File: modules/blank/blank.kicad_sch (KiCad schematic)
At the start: 2 parts

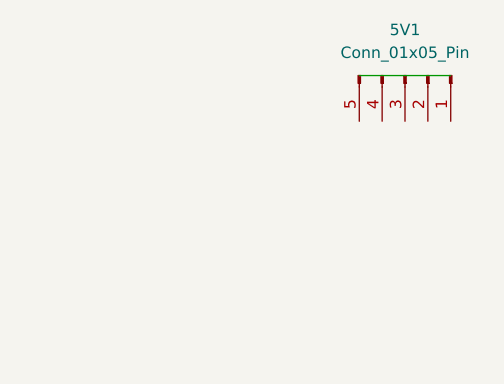
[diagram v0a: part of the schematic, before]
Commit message: Fixed some pcb layout issues.
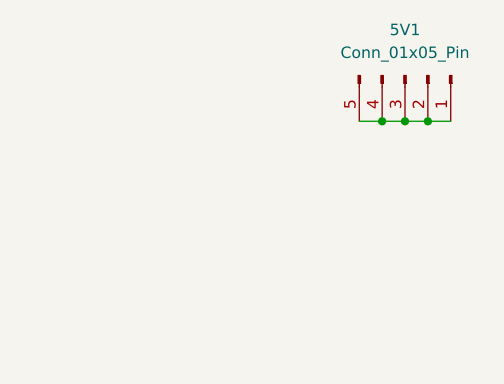
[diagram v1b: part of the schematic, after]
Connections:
- net at 5V1.1 (Pin_1): now also 5V1.2 (Pin_2), 5V1.3 (Pin_3), 5V1.4 (Pin_4), 5V1.5 (Pin_5)
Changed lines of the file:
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@@
+	)
+	(junction
+		(at 139.7 40.64)
+		(diameter 0)
+		(color 0 0 0 0)
 	)
 	(junction
 		(at 38.1 125.73)
+		(diameter 0)
+		(color 0 0 0 0)
+	)
+	(junction
+		(at 144.78 40.64)
+		(diameter 0)
+		(color 0 0 0 0)
+	)
+	(junction
+		(at 142.24 40.64)
 		(diameter 0)
 		(color 0 0 0 0)
@@
 	(wire
 		(pts
-			(xy 137.16 35.56) (xy 147.32 35.56)
+			(xy 137.16 40.64) (xy 139.7 40.64)
 		)
 		(stroke
@@
 	(wire
 		(pts
+			(xy 139.7 40.64) (xy 142.24 40.64)
+		)
+		(stroke
+			(width 0)
+			(type default)
+		)
+	)
+	(wire
+		(pts
 			(xy 38.1 125.73) (xy 40.64 125.73)
 		)
 		(stroke
+			(width 0)
+			(type default)
+		)
+	)
+	(wire
+		(pts
+			(xy 144.78 40.64) (xy 147.32 40.64)
+		)
+		(stroke
+			(width 0)
+			(type default)
+		)
+	)
+	(wire
+		(pts
+			(xy 142.24 40.64) (xy 144.78 40.64)
+		)
+		(stroke

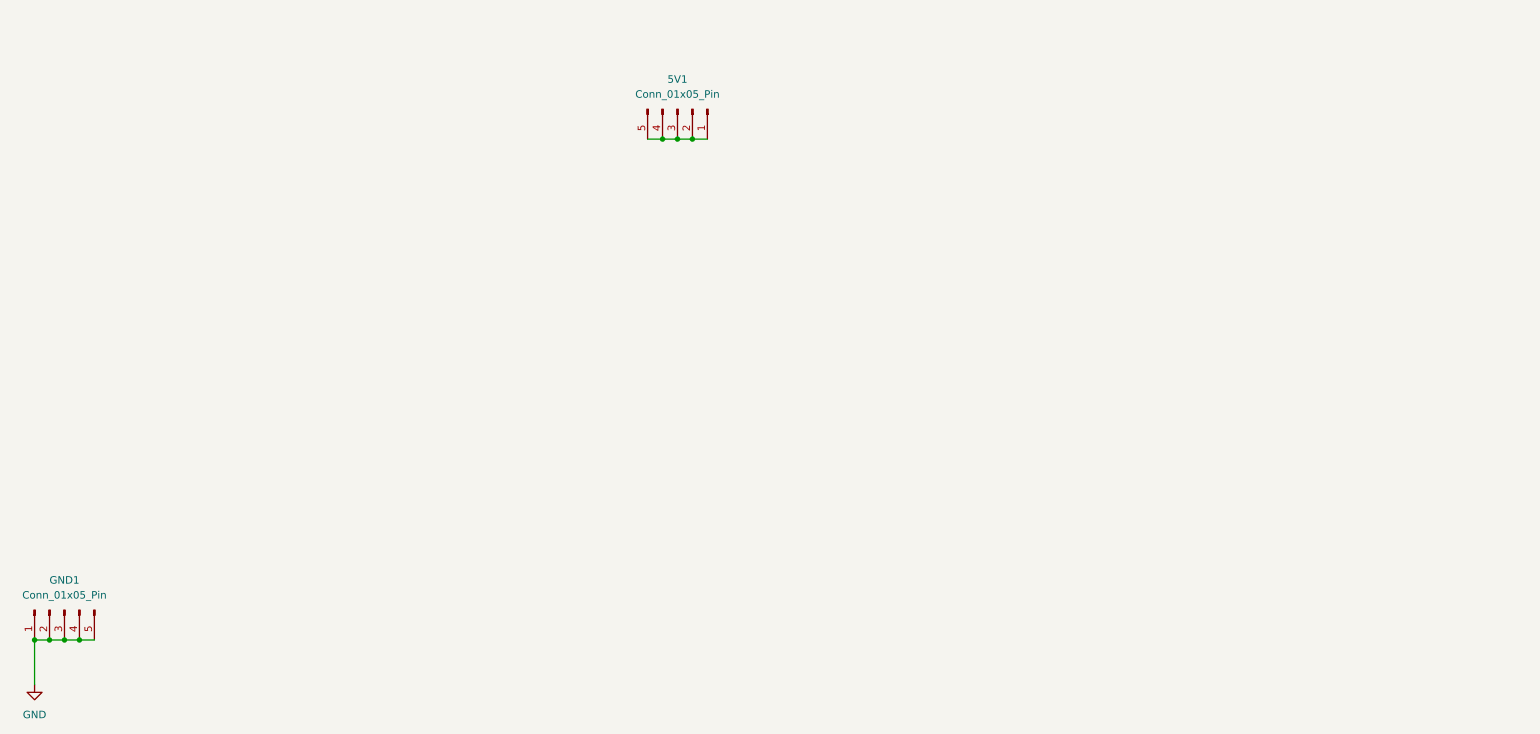
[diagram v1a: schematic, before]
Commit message: Add sockets for the blank project.
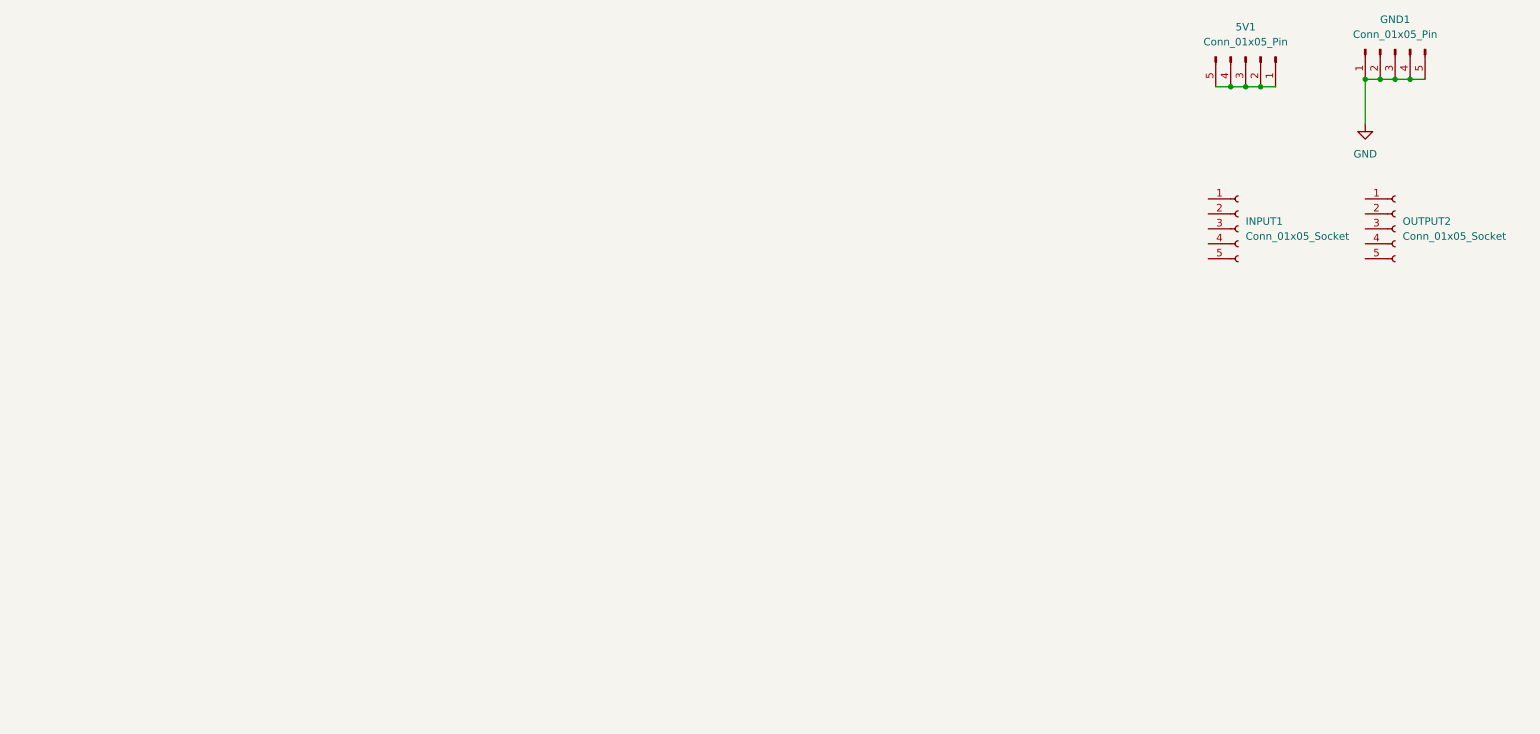
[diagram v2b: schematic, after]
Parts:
- added INPUT1, OUTPUT2: Conn_01x05_Socket, Connector_PinSocket_2.54mm:PinSocket_1x05_P2.54mm_Vertical, symbol Connector:Conn_01x05_Socket
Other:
- moved on the sheet: 5V1, GND1

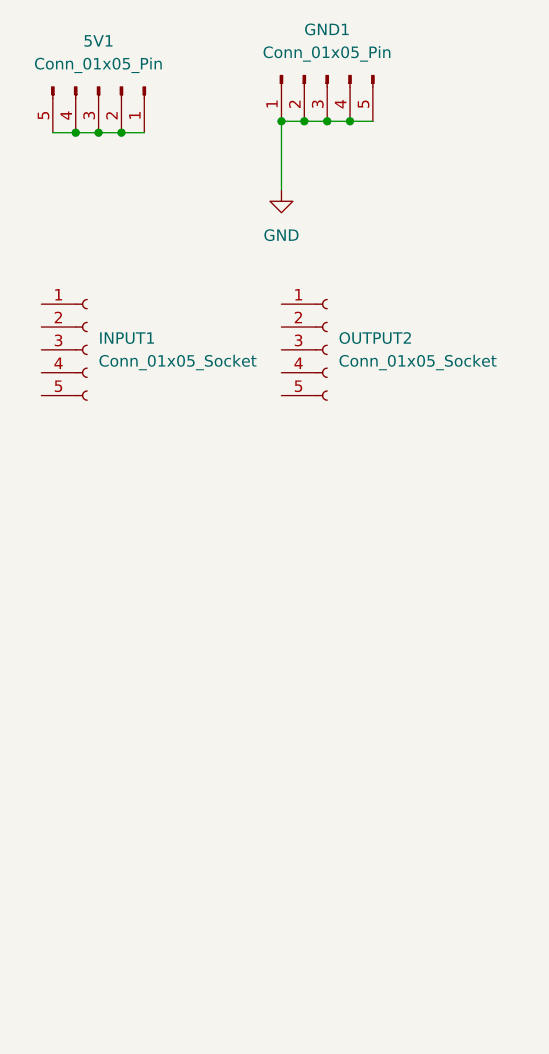
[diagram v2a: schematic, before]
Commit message: Update the basic kidcad app Add simulation support Introduce the version number silkscreen
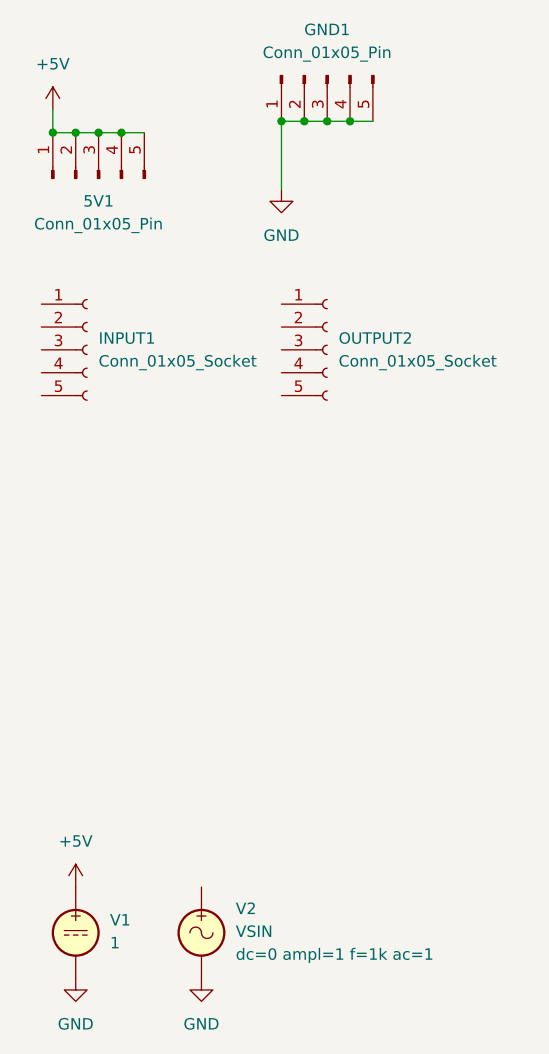
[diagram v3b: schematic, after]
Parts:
- added V1: 1, symbol Simulation_SPICE:VDC
- added V2: VSIN, symbol Simulation_SPICE:VSIN
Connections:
- net GND: now also V1.2, V2.2
- net +5V: now reaches 5V1.1 (Pin_1), 5V1.2 (Pin_2), 5V1.3 (Pin_3), 5V1.4 (Pin_4), 5V1.5 (Pin_5)
- net +5V: now also V1.1
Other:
- moved on the sheet: 5V1

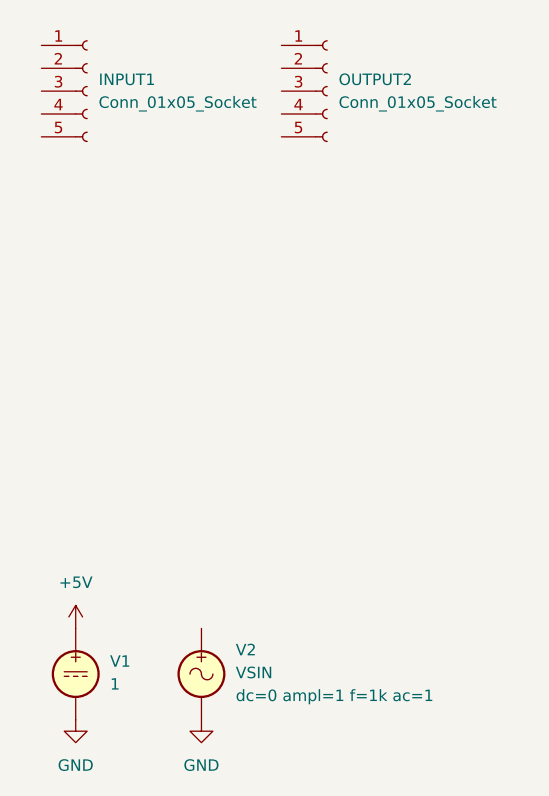
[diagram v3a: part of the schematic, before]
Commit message: Update the blank module with more details.
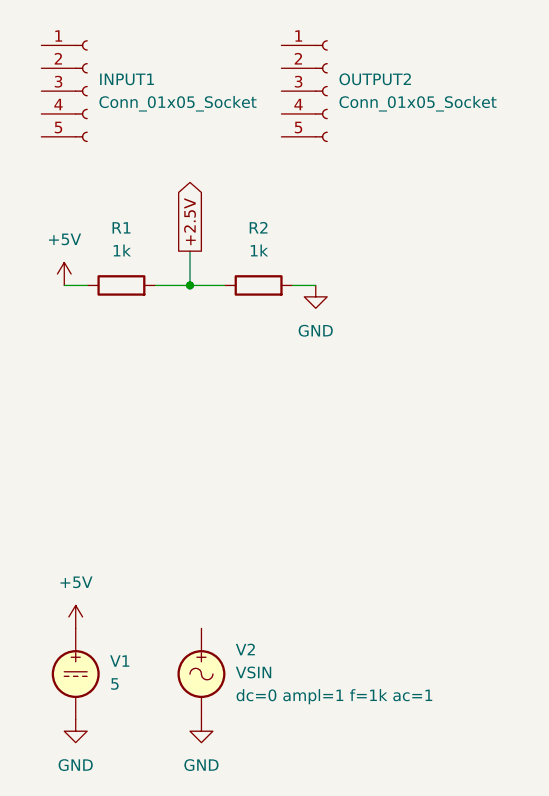
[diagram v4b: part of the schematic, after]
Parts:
- added R1, R2: 1k, symbol Device:R
- V1: value 1 -> 5
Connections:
- net +5V: now also R1.1
- net GND: now also R2.2
- new net +2.5V: R1.2, R2.1

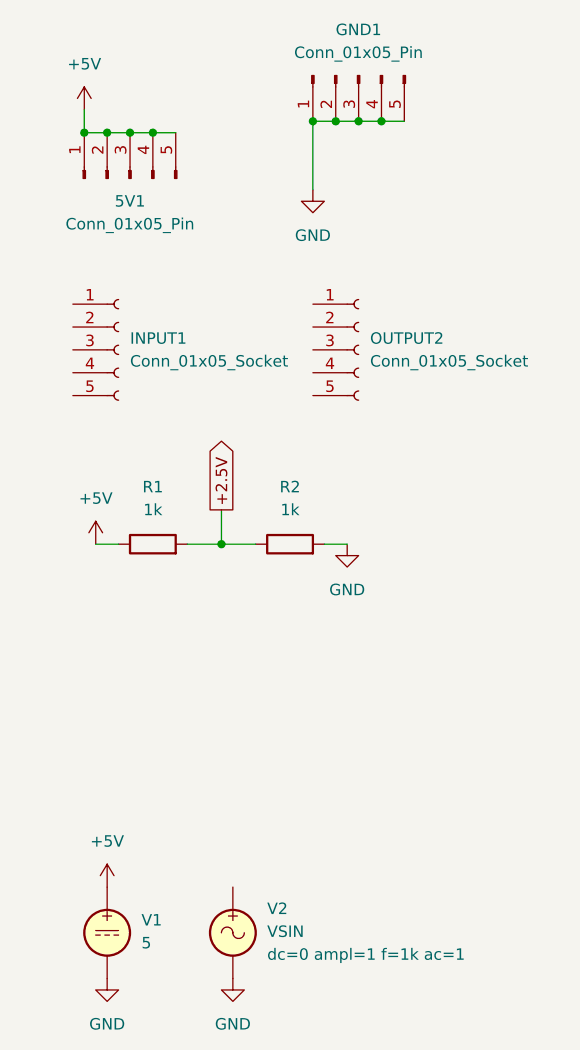
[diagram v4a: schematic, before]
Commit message: Update the blank module.
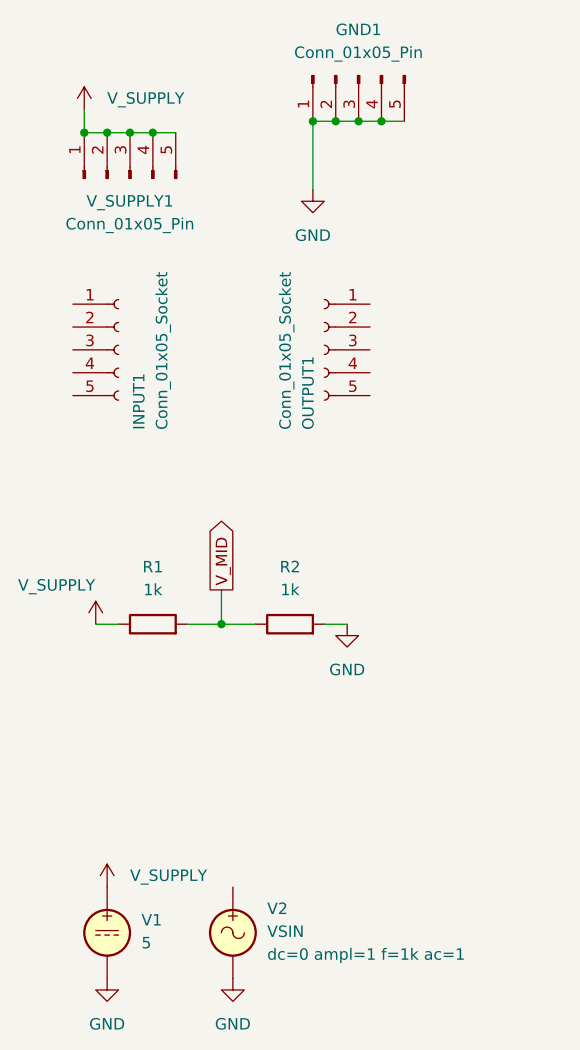
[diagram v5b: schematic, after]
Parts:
- GND1: footprint Connector_PinHeader_2.54mm:PinHeader_1x05_P2.54mm_Vertical -> BreadModular_MISC:Power_Connector
- V_SUPPLY1: renamed from 5V1; footprint Connector_PinHeader_2.54mm:PinHeader_1x05_P2.54mm_Vertical -> BreadModular_MISC:Power_Connector
- renumbered OUTPUT2 to OUTPUT1
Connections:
- net +2.5V renamed V_MID
- net +5V renamed V_SUPPLY
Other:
- moved on the sheet: OUTPUT1, R1, R2
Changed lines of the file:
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@@
 	)
 	(junction
-		(at 248.92 77.47)
+		(at 248.92 86.36)
 		(diameter 0)
 		(color 0 0 0 0)
@@
 	(wire
 		(pts
-			(xy 248.92 73.66) (xy 248.92 77.47)
-		)
-		(stroke
-			(width 0)
-			(type default)
-		)
-	)
-	(wire
-		(pts
-			(xy 248.92 77.47) (xy 252.73 77.47)
+			(xy 248.92 82.55) (xy 248.92 86.36)
+		)
+		(stroke
+			(width 0)
+			(type default)
+		)
+	)
+	(wire
+		(pts
+			(xy 248.92 86.36) (xy 252.73 86.36)
 		)
 		(stroke
@@
 	(wire
 		(pts
-			(xy 262.89 77.47) (xy 260.35 77.47)
+			(xy 262.89 86.36) (xy 260.35 86.36)
 		)
 		(stroke
@@
 	(wire
 		(pts
-			(xy 234.95 77.47) (xy 237.49 77.47)
+			(xy 234.95 86.36) (xy 237.49 86.36)
 		)
 		(stroke
@@
 	(wire
 		(pts
-			(xy 245.11 77.47) (xy 248.92 77.47)
+			(xy 245.11 86.36) (xy 248.92 86.36)
 		)
 		(stroke
@@
 		)
 	)
-	(global_label "+2.5V"
+	(global_label "V_MID"
 		(shape output)
-		(at 248.92 73.66 90)
+		(at 248.92 82.55 90)
 		(fields_autoplaced yes)
 		(effects
@@
 		)
 		(property "Intersheetrefs" "${INTERSHEET_REFS}"
-			(at 248.92 64.99 90)
+			(at 248.92 74.1824 90)
 			(effects
 				(font
@@
 	(symbol
 		(lib_id "Device:R")
-		(at 241.3 77.47 90)
+		(at 241.3 86.36 90)
 		(unit 1)
 		(exclude_from_sim no)
@@
 		(fields_autoplaced yes)
 		(property "Reference" "R1"
-			(at 241.3 71.12 90)
+			(at 241.3 80.01 90)
 			(effects
 				(font
@@
 		)
 		(property "Value" "1k"
-			(at 241.3 73.66 90)
+			(at 241.3 82.55 90)
 			(effects
 				(font
@@
 		)
 		(property "Footprint" ""
-			(at 241.3 79.248 90)
+			(at 241.3 88.138 90)
 			(effects
 				(font
@@
 		)
 		(property "Datasheet" "~"
-			(at 241.3 77.47 0)
+			(at 241.3 86.36 0)
 			(effects
 				(font
@@
 		)
 		(property "Description" "Resistor"
-			(at 241.3 77.47 0)
+			(at 241.3 86.36 0)
 			(effects
 				(font
@@
 		(dnp no)
 		(fields_autoplaced yes)
-		(property "Reference" "5V1"
+		(property "Reference" "V_SUPPLY1"
 			(at 238.76 39.37 90)
 			(effects
@@
 			)
 		)
-		(property "Footprint" "Connector_PinHeader_2.54mm:PinHeader_1x05_P2.54mm_Vertical"
+		(property "Footprint" "BreadModular_MISC:Power_Connector"
 			(at 238.76 36.83 0)
 			(effects
@@
 			(project ""
 				(path "/b63493d3-5f6d-47e3-845b-87e7090fc1ab"
-					(reference "5V1")
+					(reference "V_SUPPLY1")
 					(unit 1)
 				)
@@
 			)
 		)
-		(property "Value" "+5V"
-			(at 236.22 110.49 0)
-			(effects
-				(font
-					(size 1.27 1.27)
-				)
+		(property "Value" "V_SUPPLY"
+			(at 238.76 114.2999 0)
+			(effects
+				(font
+					(size 1.27 1.27)
+				)
+				(justify left)
 			)
 		)
@@
 			)
 		)
-		(property "Value" "+5V"
-			(at 233.68 24.13 0)
-			(effects
-				(font
-					(size 1.27 1.27)
-				)
+		(property "Value" "V_SUPPLY"
+			(at 236.22 27.9399 0)
+			(effects
+				(font
+					(size 1.27 1.27)
+				)
+				(justify left)
 			)
 		)
@@
 	(symbol
 		(lib_id "Connector:Conn_01x05_Socket")
-		(at 264.16 55.88 0)
+		(at 260.35 55.88 0)
+		(mirror y)
 		(unit 1)
 		(exclude_from_sim yes)
@@
 		(on_board yes)
 		(dnp no)
-		(fields_autoplaced yes)
-		(property "Reference" "OUTPUT2"
-			(at 265.43 54.6099 0)
+		(property "Reference" "OUTPUT1"
+			(at 258.572 64.77 90)
 			(effects
 				(font
@@
 		)
 		(property "Value" "Conn_01x05_Socket"
-			(at 265.43 57.1499 0)
+			(at 256.032 64.77 90)
 			(effects
 				(font
@@
 		)
 		(property "Footprint" "Connector_PinSocket_2.54mm:PinSocket_1x05_P2.54mm_Vertical"
-			(at 264.16 55.88 0)
+			(at 260.35 55.88 0)
 			(effects
 				(font
@@
 		)
 		(property "Datasheet" "~"
-			(at 264.16 55.88 0)
+			(at 260.35 55.88 0)
 			(effects
 				(font
@@
 		)
 		(property "Description" "Generic connector, single row, 01x05, script generated"
-			(at 264.16 55.88 0)
+			(at 260.35 55.88 0)
 			(effects
 				(font
@@
 			(project "blank"
 				(path "/b63493d3-5f6d-47e3-845b-87e7090fc1ab"
-					(reference "OUTPUT2")
+					(reference "OUTPUT1")
 					(unit 1)
 				)
@@
 	(symbol
 		(lib_id "power:GND")
-		(at 262.89 77.47 0)
+		(at 262.89 86.36 0)
 		(unit 1)
 		(exclude_from_sim no)
@@
 		(dnp no)
 		(property "Reference" "#PWR07"
-			(at 262.89 83.82 0)
+			(at 262.89 92.71 0)
 			(effects
 				(font
@@
 		)
 		(property "Value" "GND"
-			(at 262.89 82.55 0)
+			(at 262.89 91.44 0)
 			(effects
 				(font
@@
 		)
 		(property "Footprint" ""
-			(at 262.89 77.47 0)
+			(at 262.89 86.36 0)
 			(effects
 				(font
@@
 		)
 		(property "Datasheet" ""
-			(at 262.89 77.47 0)
+			(at 262.89 86.36 0)
 			(effects
 				(font
@@
 		)
 		(property "Description" "Power symbol creates a global label with name \"GND\" , ground"
-			(at 262.89 77.47 0)
+			(at 262.89 86.36 0)
 			(effects
 				(font
@@
 	(symbol
 		(lib_id "Device:R")
-		(at 256.54 77.47 90)
+		(at 256.54 86.36 90)
 		(unit 1)
 		(exclude_from_sim no)
@@
 		(fields_autoplaced yes)
 		(property "Reference" "R2"
-			(at 256.54 71.12 90)
+			(at 256.54 80.01 90)
 			(effects
 				(font
@@
 		)
 		(property "Value" "1k"
-			(at 256.54 73.66 90)
+			(at 256.54 82.55 90)
 			(effects
 				(font
@@
 		)
 		(property "Footprint" ""
-			(at 256.54 79.248 90)
+			(at 256.54 88.138 90)
 			(effects
 				(font
@@
 		)
 		(property "Datasheet" "~"
-			(at 256.54 77.47 0)
+			(at 256.54 86.36 0)
 			(effects
 				(font
@@
 		)
 		(property "Description" "Resistor"
-			(at 256.54 77.47 0)
+			(at 256.54 86.36 0)
 			(effects
 				(font
@@
 		(on_board yes)
 		(dnp no)
-		(fields_autoplaced yes)
 		(property "Reference" "INPUT1"
-			(at 238.76 54.6099 0)
+			(at 239.776 64.77 90)
 			(effects
 				(font
@@
 		)
 		(property "Value" "Conn_01x05_Socket"
-			(at 238.76 57.1499 0)
+			(at 242.316 64.77 90)
 			(effects
 				(font
@@
 			)
 		)
-		(property "Footprint" "Connector_PinHeader_2.54mm:PinHeader_1x05_P2.54mm_Vertical"
+		(property "Footprint" "BreadModular_MISC:Power_Connector"
 			(at 264.16 25.4 0)
 			(effects
@@
 	(symbol
 		(lib_id "power:+5V")
-		(at 234.95 77.47 0)
+		(at 234.95 86.36 0)
 		(unit 1)
 		(exclude_from_sim no)
@@
 		(on_board yes)
 		(dnp no)
-		(fields_autoplaced yes)
 		(property "Reference" "#PWR06"
-			(at 234.95 81.28 0)
-			(effects
-				(font
-					(size 1.27 1.27)
-				)
-				(hide yes)
-			)
-		)
-		(property "Value" "+5V"
-			(at 234.95 72.39 0)
-			(effects
-				(font
-					(size 1.27 1.27)
-				)
+			(at 234.95 90.17 0)
+			(effects
+				(font
+					(size 1.27 1.27)
+				)
+				(hide yes)
+			)
+		)
+		(property "Value" "V_SUPPLY"
+			(at 226.314 82.042 0)
+			(effects
+				(font
+					(size 1.27 1.27)
+				)
+				(justify left)
 			)
 		)
 		(property "Footprint" ""
-			(at 234.95 77.47 0)
+			(at 234.95 86.36 0)
 			(effects
 				(font
@@
 		)
 		(property "Datasheet" ""
-			(at 234.95 77.47 0)
+			(at 234.95 86.36 0)
 			(effects
 				(font
@@
 		)
 		(property "Description" "Power symbol creates a global label with name \"+5V\""
-			(at 234.95 77.47 0)
-			(effects
-				(font
+			(at 234.95 86.36 0)
+			(effects
+				(font
